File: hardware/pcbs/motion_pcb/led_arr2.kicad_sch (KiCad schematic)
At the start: 21 parts

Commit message: finished schematic
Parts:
- removed C5: 10v/1mF, Capacitor_SMD:CP_Elec_10x10, symbol Device:C_Polarized
- removed D1, D10, D11, D12, D13, D14, D15, D16, D17, D18, D19, D2, D3, D4, D5, D6, D7, D8, D9: WS2812B-2020, LED_SMD:LED_WS2812B-2020_PLCC4_2.0x2.0mm, symbol 3dAudioSym:A3_switches_led
- removed D20: switches, 3dAudioFoot:A3_CherryMxHybrid_WS2812Led2020, symbol 3dAudioSym:A3_switches_led
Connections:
- no-connect marks 1 -> 0
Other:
- added sheet LED_Button (led_button_h.kicad_sch)
- added sheet LED_Button1 (led_button_h.kicad_sch)
- added sheet LED_Button10 (led_button_h.kicad_sch)
- added sheet LED_Button11 (led_button_h.kicad_sch)
- added sheet LED_Button12 (led_button_h.kicad_sch)
- added sheet LED_Button13 (led_button_h.kicad_sch)
- added sheet LED_Button14 (led_button_h.kicad_sch)
- added sheet LED_Button15 (led_button_h.kicad_sch)
- added sheet LED_Button2 (led_button_h.kicad_sch)
- added sheet LED_Button3 (led_button_h.kicad_sch)
- added sheet LED_Button4 (led_button_h.kicad_sch)
- added sheet LED_Button5 (led_button_h.kicad_sch)
- added sheet LED_Button6 (led_button_h.kicad_sch)
- added sheet LED_Button7 (led_button_h.kicad_sch)
- added sheet LED_Button8 (led_button_h.kicad_sch)
- added sheet LED_Button9 (led_button_h.kicad_sch)

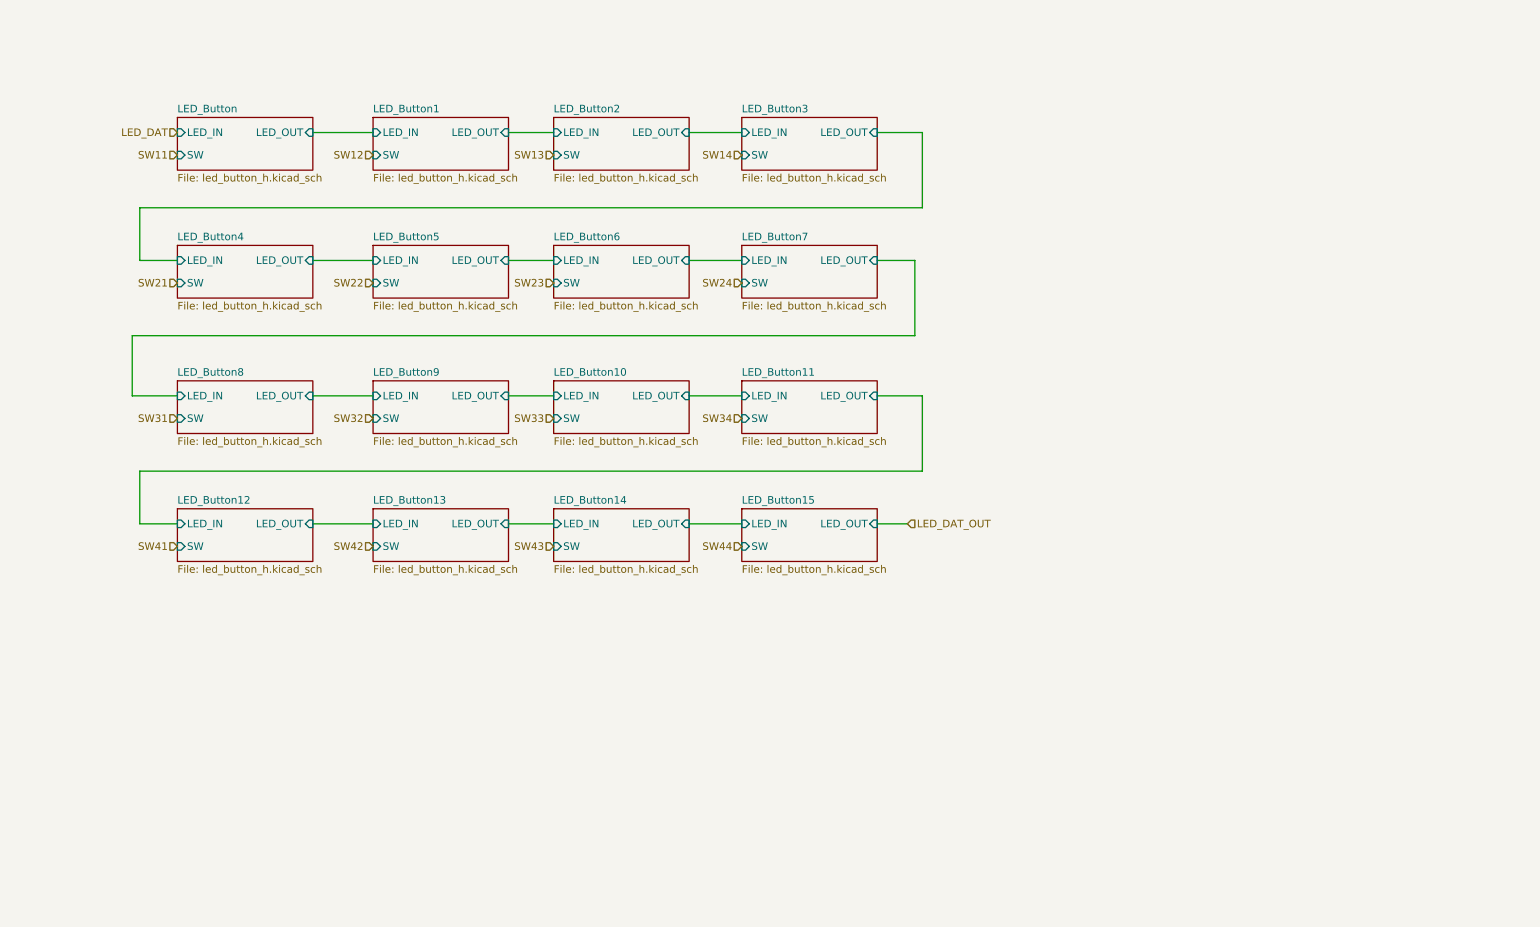
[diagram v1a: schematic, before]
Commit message: changing labels
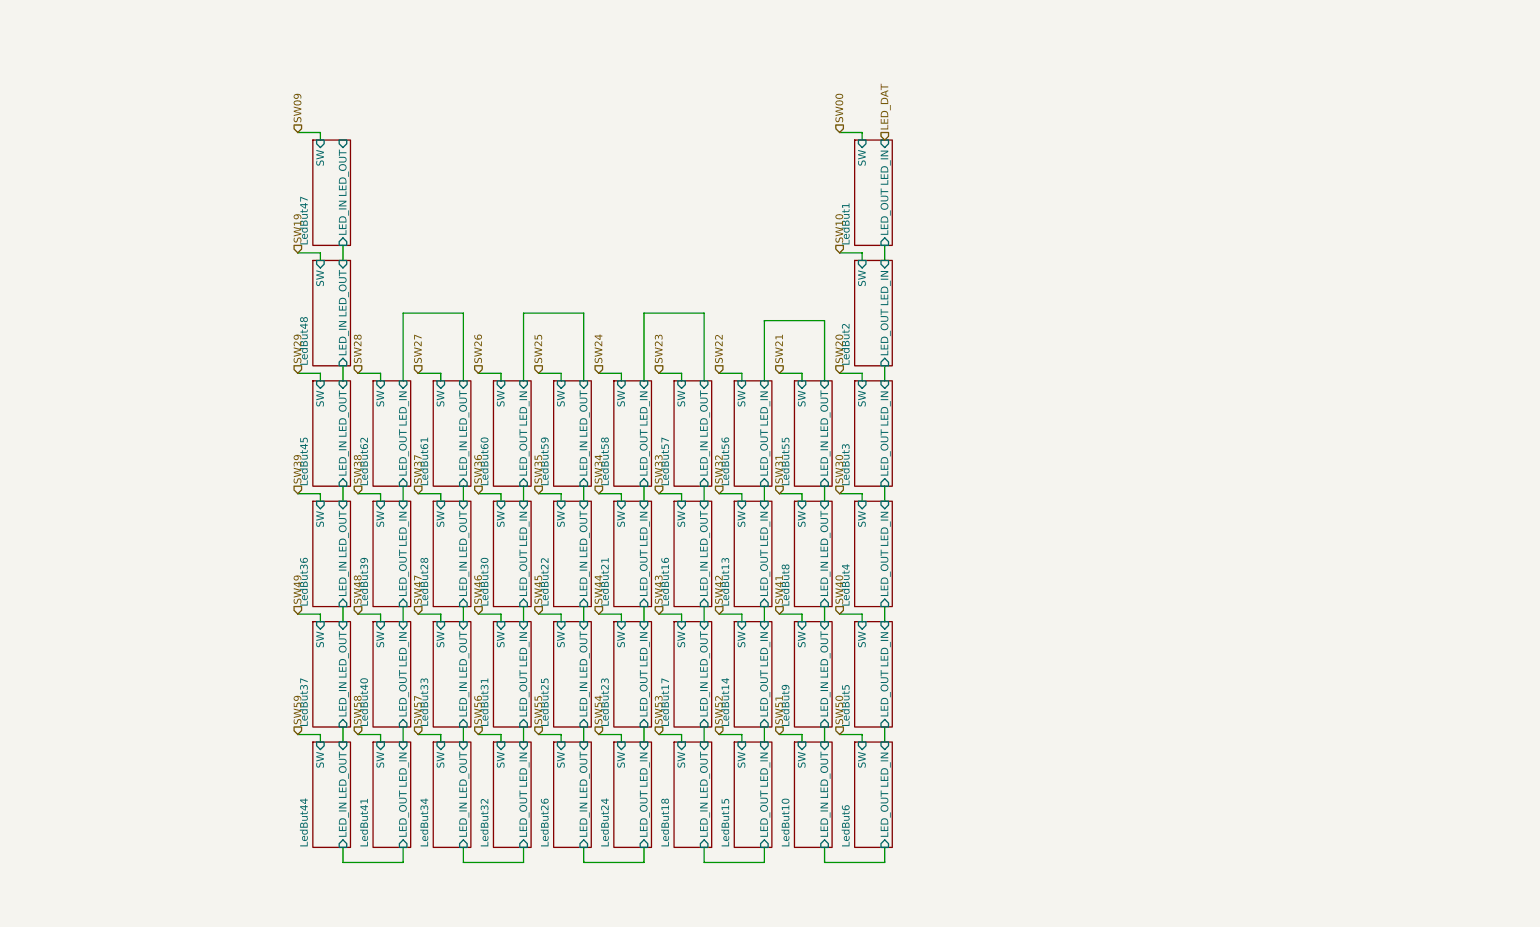
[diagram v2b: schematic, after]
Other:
- removed sheet LED_Button
- removed sheet LED_Button1
- removed sheet LED_Button10
- removed sheet LED_Button11
- removed sheet LED_Button12
- removed sheet LED_Button13
- removed sheet LED_Button14
- removed sheet LED_Button15
- removed sheet LED_Button2
- removed sheet LED_Button3
- removed sheet LED_Button4
- removed sheet LED_Button5
- removed sheet LED_Button6
- removed sheet LED_Button7
- removed sheet LED_Button8
- removed sheet LED_Button9
- added sheet LedBut1 (led_but/led_but.kicad_sch)
- added sheet LedBut10 (led_but/led_but.kicad_sch)
- added sheet LedBut13 (led_but/led_but.kicad_sch)
- added sheet LedBut14 (led_but/led_but.kicad_sch)
- added sheet LedBut15 (led_but/led_but.kicad_sch)
- added sheet LedBut16 (led_but/led_but.kicad_sch)
- added sheet LedBut17 (led_but/led_but.kicad_sch)
- added sheet LedBut18 (led_but/led_but.kicad_sch)
- added sheet LedBut2 (led_but/led_but.kicad_sch)
- added sheet LedBut21 (led_but/led_but.kicad_sch)
- added sheet LedBut22 (led_but/led_but.kicad_sch)
- added sheet LedBut23 (led_but/led_but.kicad_sch)
- added sheet LedBut24 (led_but/led_but.kicad_sch)
- added sheet LedBut25 (led_but/led_but.kicad_sch)
- added sheet LedBut26 (led_but/led_but.kicad_sch)
- added sheet LedBut28 (led_but/led_but.kicad_sch)
- added sheet LedBut3 (led_but/led_but.kicad_sch)
- added sheet LedBut30 (led_but/led_but.kicad_sch)
- added sheet LedBut31 (led_but/led_but.kicad_sch)
- added sheet LedBut32 (led_but/led_but.kicad_sch)
- added sheet LedBut33 (led_but/led_but.kicad_sch)
- added sheet LedBut34 (led_but/led_but.kicad_sch)
- added sheet LedBut36 (led_but/led_but.kicad_sch)
- added sheet LedBut37 (led_but/led_but.kicad_sch)
- added sheet LedBut39 (led_but/led_but.kicad_sch)
- added sheet LedBut4 (led_but/led_but.kicad_sch)
- added sheet LedBut40 (led_but/led_but.kicad_sch)
- added sheet LedBut41 (led_but/led_but.kicad_sch)
- added sheet LedBut44 (led_but/led_but.kicad_sch)
- added sheet LedBut45 (led_but/led_but.kicad_sch)
- added sheet LedBut47 (led_but/led_but.kicad_sch)
- added sheet LedBut48 (led_but/led_but.kicad_sch)
- added sheet LedBut5 (led_but/led_but.kicad_sch)
- added sheet LedBut55 (led_but/led_but.kicad_sch)
- added sheet LedBut56 (led_but/led_but.kicad_sch)
- added sheet LedBut57 (led_but/led_but.kicad_sch)
- added sheet LedBut58 (led_but/led_but.kicad_sch)
- added sheet LedBut59 (led_but/led_but.kicad_sch)
- added sheet LedBut6 (led_but/led_but.kicad_sch)
- added sheet LedBut60 (led_but/led_but.kicad_sch)
- added sheet LedBut61 (led_but/led_but.kicad_sch)
- added sheet LedBut62 (led_but/led_but.kicad_sch)
- added sheet LedBut8 (led_but/led_but.kicad_sch)
- added sheet LedBut9 (led_but/led_but.kicad_sch)

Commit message: finished design
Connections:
- no-connect marks 0 -> 1
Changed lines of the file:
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@@
 	(generator_version "9.0")
 	(paper "A4")
+	(no_connect
+		(at 72.39 33.02)
+	)
 	(wire
 		(pts
